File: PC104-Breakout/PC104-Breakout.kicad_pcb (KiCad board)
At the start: 2 copper layers, 175 x 131 mm, 59 parts, among them J1 H1-02x26_Even, J10 Conn_01x02, J11 Conn_01x03_Socket, J12 Conn_01x03_Socket, J13 Conn_01x03_Socket, J2 H1-02x26_Odd, J3 H2-0x26_Even, J4 H2-0x26_Odd, J5 Screw_Terminal_01x02, J6 Screw_Terminal_01x02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

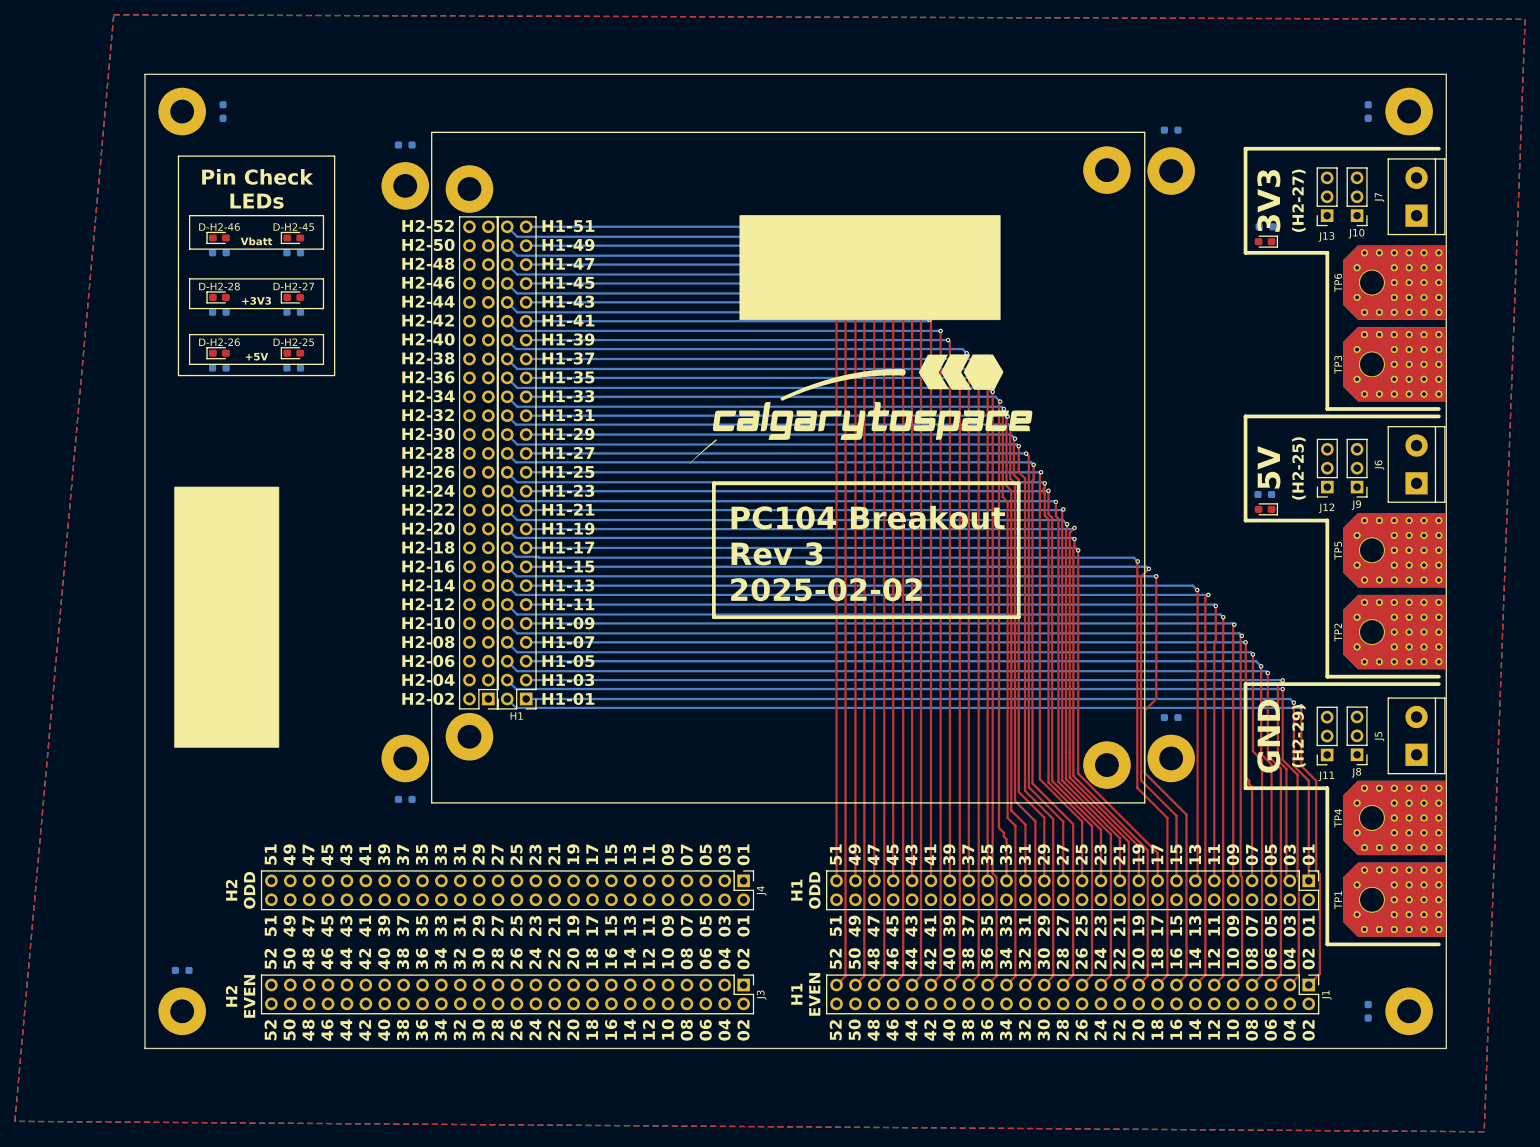
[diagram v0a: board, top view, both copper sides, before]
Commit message: Reroute H1 with breakout flipped
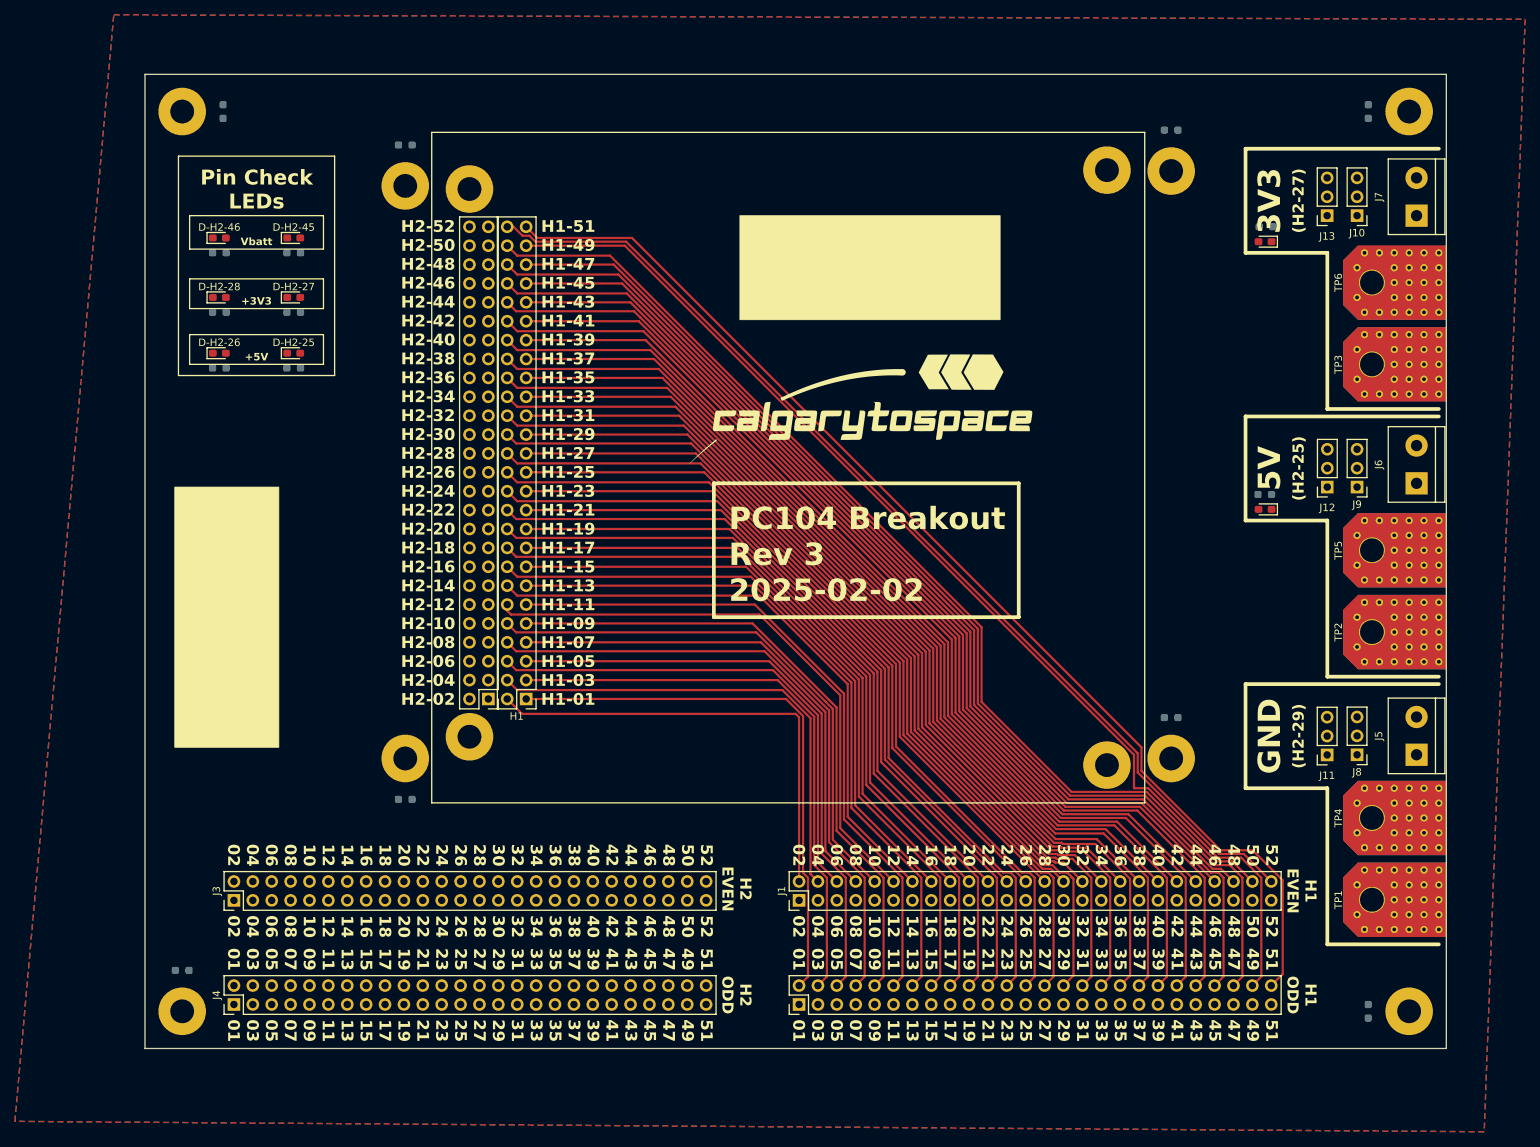
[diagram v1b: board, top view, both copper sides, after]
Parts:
- moved J4 70.5 mm to (87.0, 153.1), turned to 90 degrees
- moved J2 70.5 mm to (163.0, 153.1), turned to 90 degrees
- moved J3 69.5 mm to (87.0, 139.1), turned to 90 degrees
- moved J1 69.5 mm to (163.0, 139.1), turned to 90 degrees
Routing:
- net H1-02: track 146.5 -> 62.3 mm, vias 1 -> 0
- net H1-04: track 146.0 -> 65.3 mm, vias 1 -> 0
- net H1-06: track 146.2 -> 68.2 mm, vias 1 -> 0
- net H1-08: track 146.5 -> 71.1 mm, vias 1 -> 0
- net H1-10: track 147.1 -> 74.1 mm, vias 1 -> 0
- net H1-12: track 146.9 -> 78.3 mm, vias 1 -> 0
- net H1-14: track 148.0 -> 81.4 mm, vias 1 -> 0
- net H1-16: track 146.3 -> 84.3 mm, vias 1 -> 0
- net H1-18: track 144.7 -> 87.3 mm, vias 1 -> 0
- net H1-01: track 128.2 -> 75.2 mm, vias 1 -> 0
- net H1-03: track 129.7 -> 78.1 mm, vias 1 -> 0
- net H1-20: track 141.5 -> 90.2 mm, vias 1 -> 0
- net H1-22: track 142.1 -> 93.1 mm, vias 1 -> 0
- net H1-05: track 128.6 -> 81.1 mm, vias 1 -> 0
- net H1-24: track 143.0 -> 96.1 mm, vias 1 -> 0
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
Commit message: Route both H1 and H2
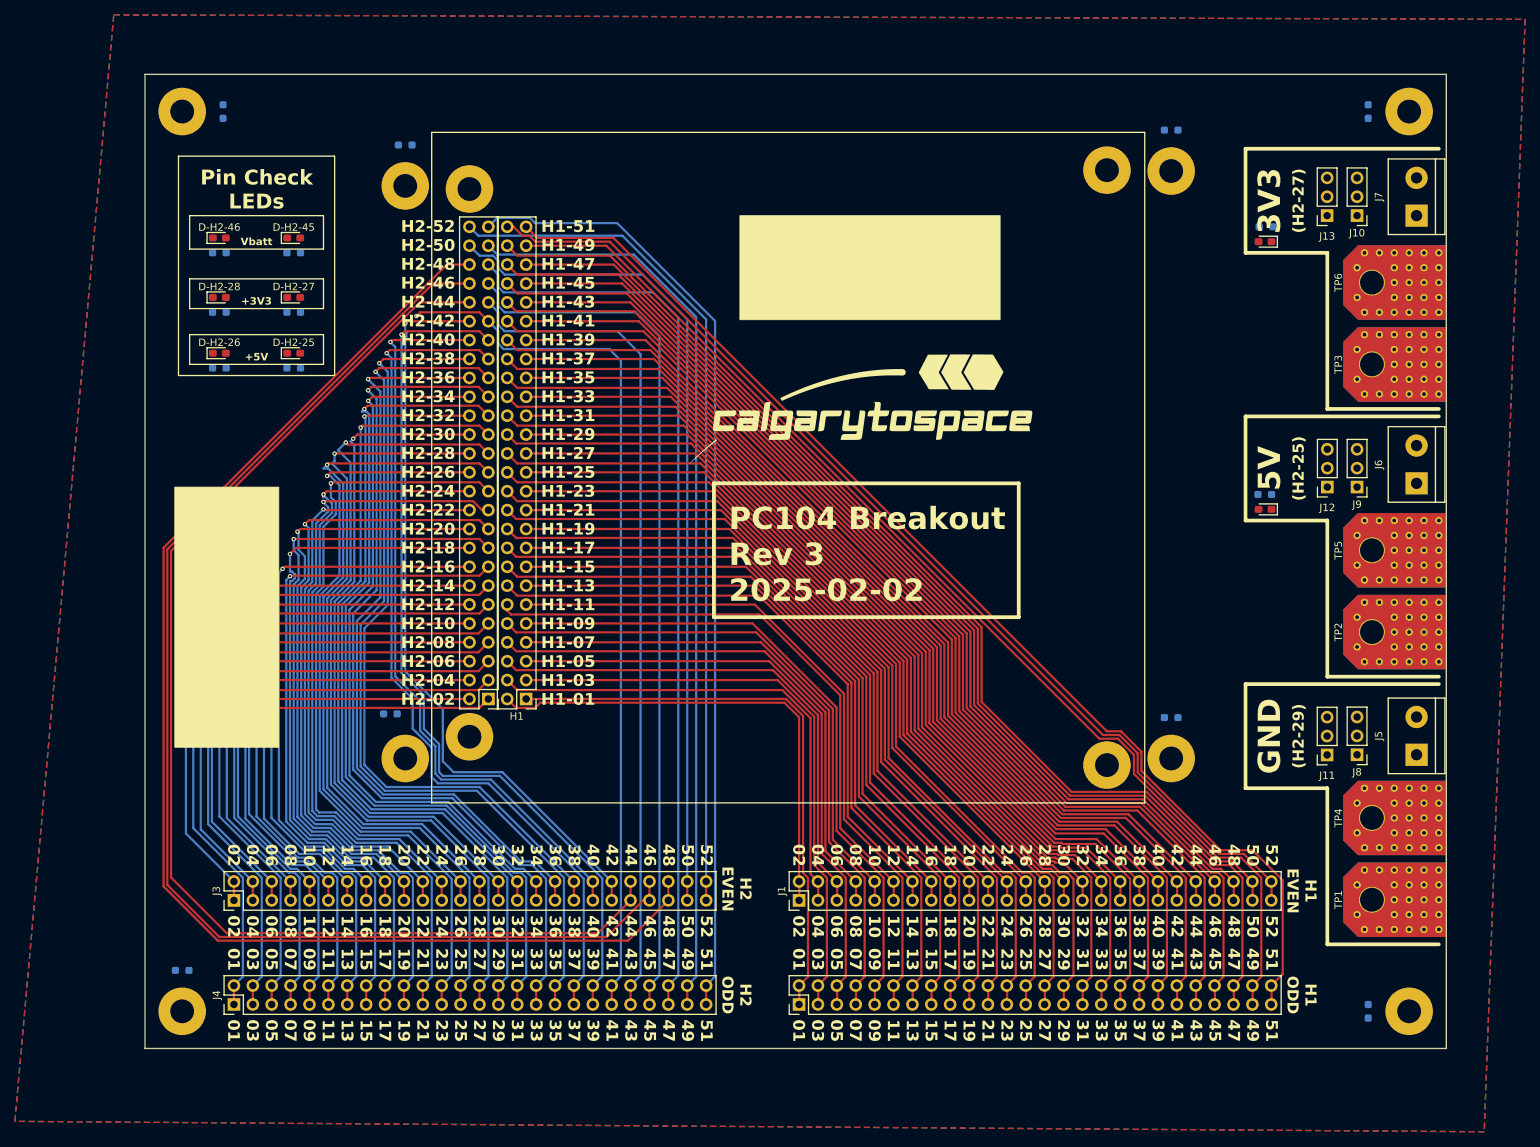
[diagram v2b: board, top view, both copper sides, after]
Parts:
- moved R5 11.7 mm to (108.0, 114.0)
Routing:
- net H2-48: track 0.00 -> 178.1 mm
- net H2-46: track 0.00 -> 174.1 mm
- net H2-44: track 0.00 -> 167.2 mm
- net H2-51: track 0.00 -> 129.1 mm
- net H2-49: track 0.00 -> 124.9 mm
- net H2-47: track 0.00 -> 122.4 mm
- net H2-35: track 0.00 -> 121.9 mm, vias 0 -> 1
- net H2-33: track 0.00 -> 119.2 mm, vias 0 -> 1
- net H2-39: track 0.00 -> 118.6 mm, vias 0 -> 1
- net H2-41: track 0.00 -> 118.6 mm, vias 0 -> 1
- net H2-37: track 0.00 -> 117.4 mm, vias 0 -> 1
- net H2-45: track 0.00 -> 117.4 mm
- net H2-31: track 0.00 -> 116.5 mm, vias 0 -> 1
- net H2-52: track 0.00 -> 115.1 mm
- net H2-43: track 0.00 -> 112.3 mm
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
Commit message: Finish Rev 3
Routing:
- net H2-25: track 110.8 -> 341.2 mm, vias 1 -> 2
- net H2-27: track 111.9 -> 311.4 mm, vias 1 -> 2
- net H2-46: track 174.1 -> 210.3 mm
- net H2-28: track 93.4 -> 124.1 mm
- net H2-45: track 117.4 -> 146.2 mm
- net H2-26: track 90.2 -> 116.2 mm
- net Net-(M9-Pad1): track 0.00 -> 7.21 mm
- net Net-(M6-Pad1): track 0.00 -> 5.88 mm
- net Net-(M5-Pad1): track 0.00 -> 5.88 mm
- net Net-(M8-Pad1): track 0.00 -> 5.88 mm
- net Net-(M7-Pad1): track 0.00 -> 5.88 mm
- net Net-(M11-Pad1): track 0.00 -> 5.88 mm
- net Net-(D7-A): track 0.00 -> 2.18 mm, vias 0 -> 1
- net Net-(D8-A): track 0.00 -> 2.17 mm, vias 0 -> 1
- net Net-(D-H2-46-A): track 0.00 -> 2.09 mm, vias 0 -> 1
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- added copper zone on B.Cu, net H2-25
- added copper zone on F.Cu, net H2-25
- added copper zone on B.Cu, net H2-27
- added copper zone on F.Cu, net H2-27

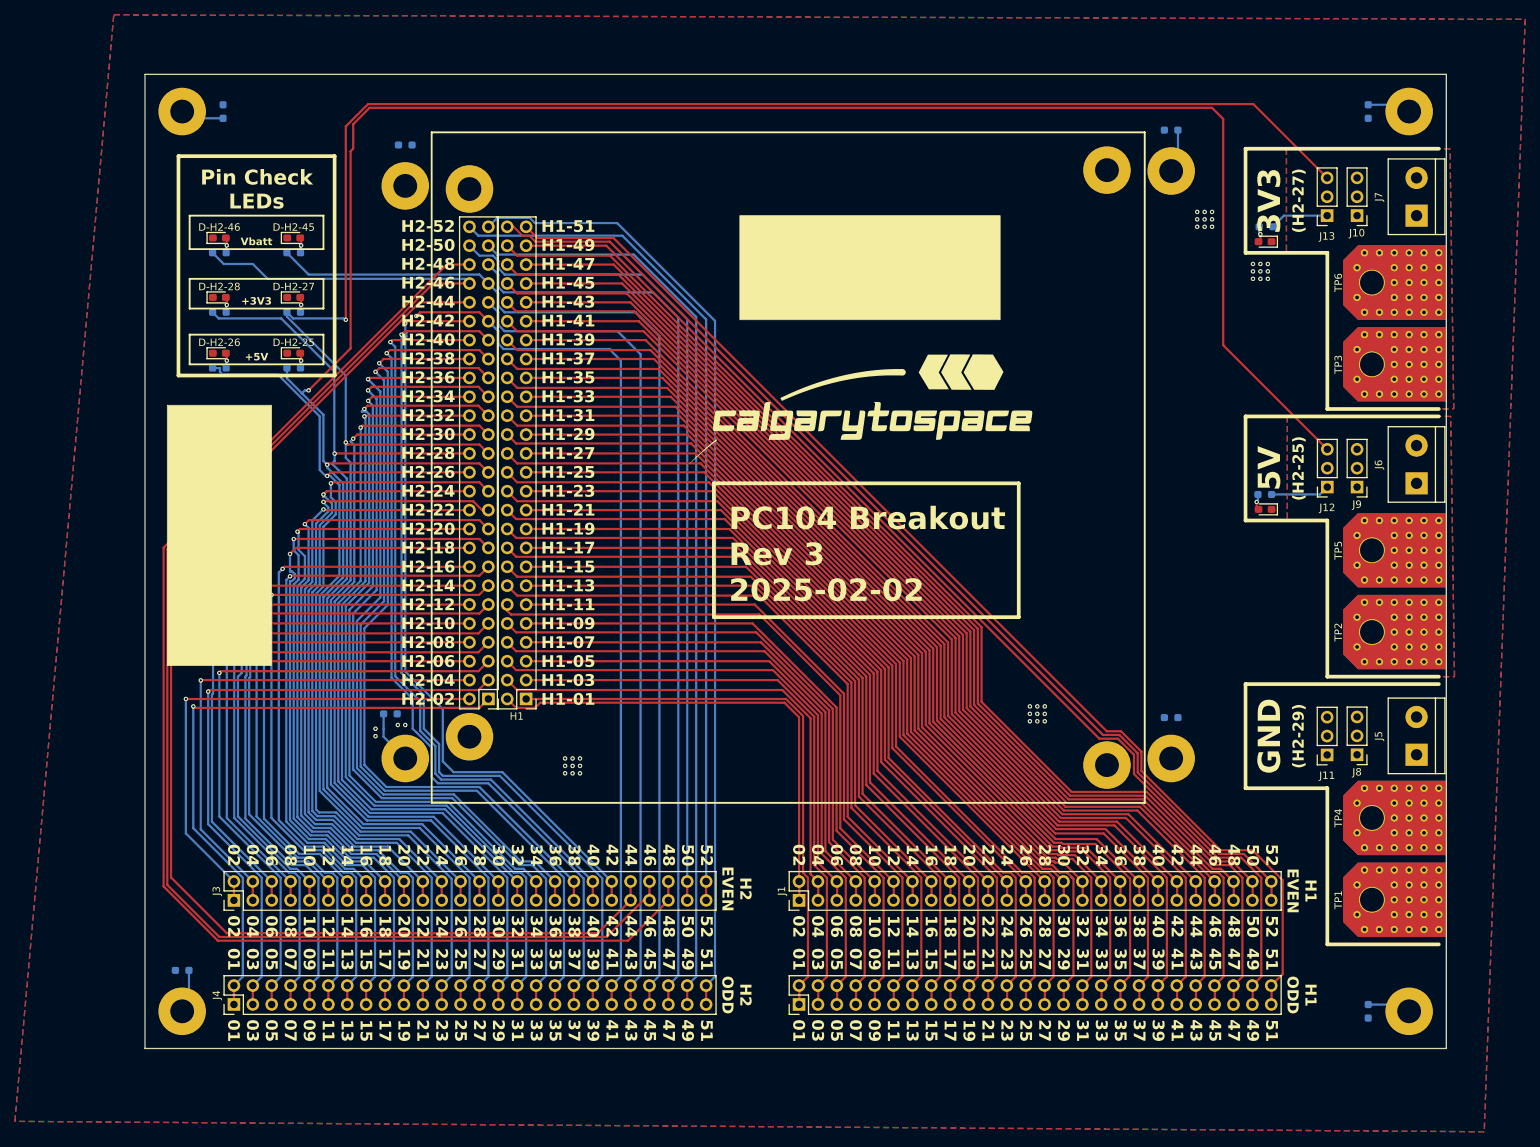
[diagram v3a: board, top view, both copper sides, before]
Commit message: Fix DRC issues - Rev 3 final
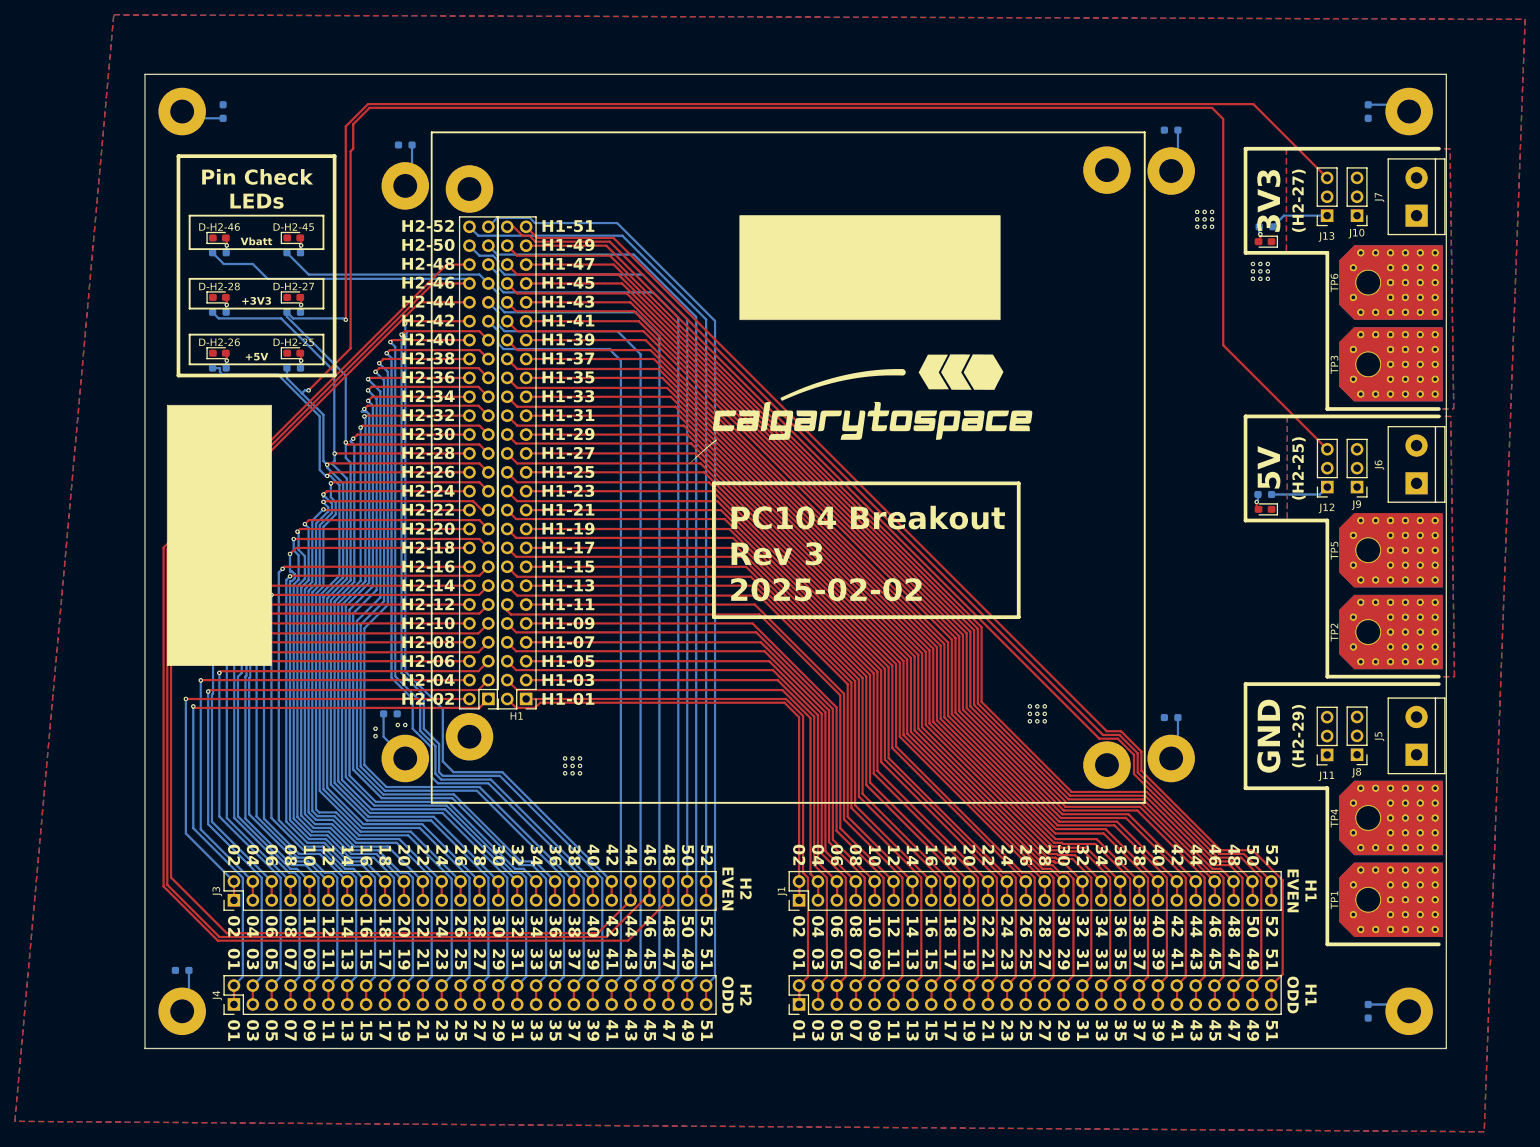
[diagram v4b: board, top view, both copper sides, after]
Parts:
- moved TP1 0.50 mm to (235.5, 139.0)
- moved TP2 0.50 mm to (235.5, 103.0)
- moved TP3 0.50 mm to (235.5, 67.0)
- moved TP4 0.50 mm to (235.5, 128.0)
- moved TP5 0.50 mm to (235.5, 92.0)
- moved TP6 0.50 mm to (235.5, 56.0)
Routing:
- net H2-41: track 118.6 -> 108.2 mm, vias 1 -> 0
- net Net-(M10-Pad1): track 0.00 -> 5.88 mm
- net Net-(M12-Pad1): track 0.00 -> 5.88 mm
